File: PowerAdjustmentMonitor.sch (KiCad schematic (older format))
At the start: 37 parts, among them U6 LM317, U7 LM317, U8 LM337T, U9 LM337T

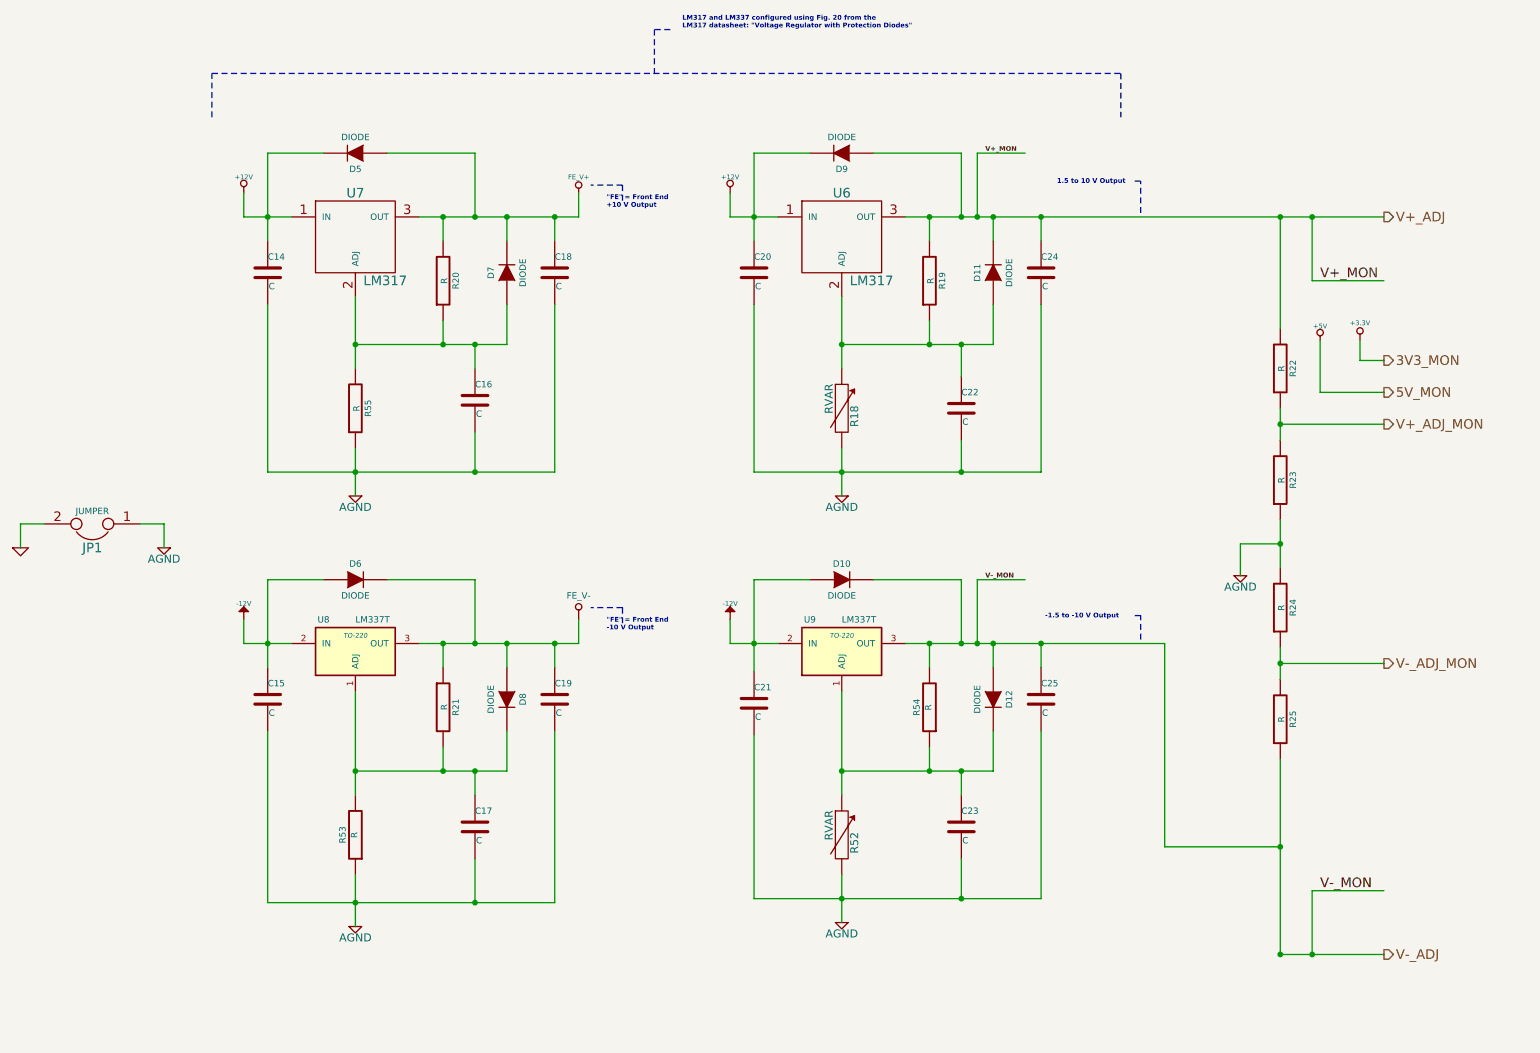
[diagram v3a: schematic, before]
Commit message: Association and layout of the power regulator mod
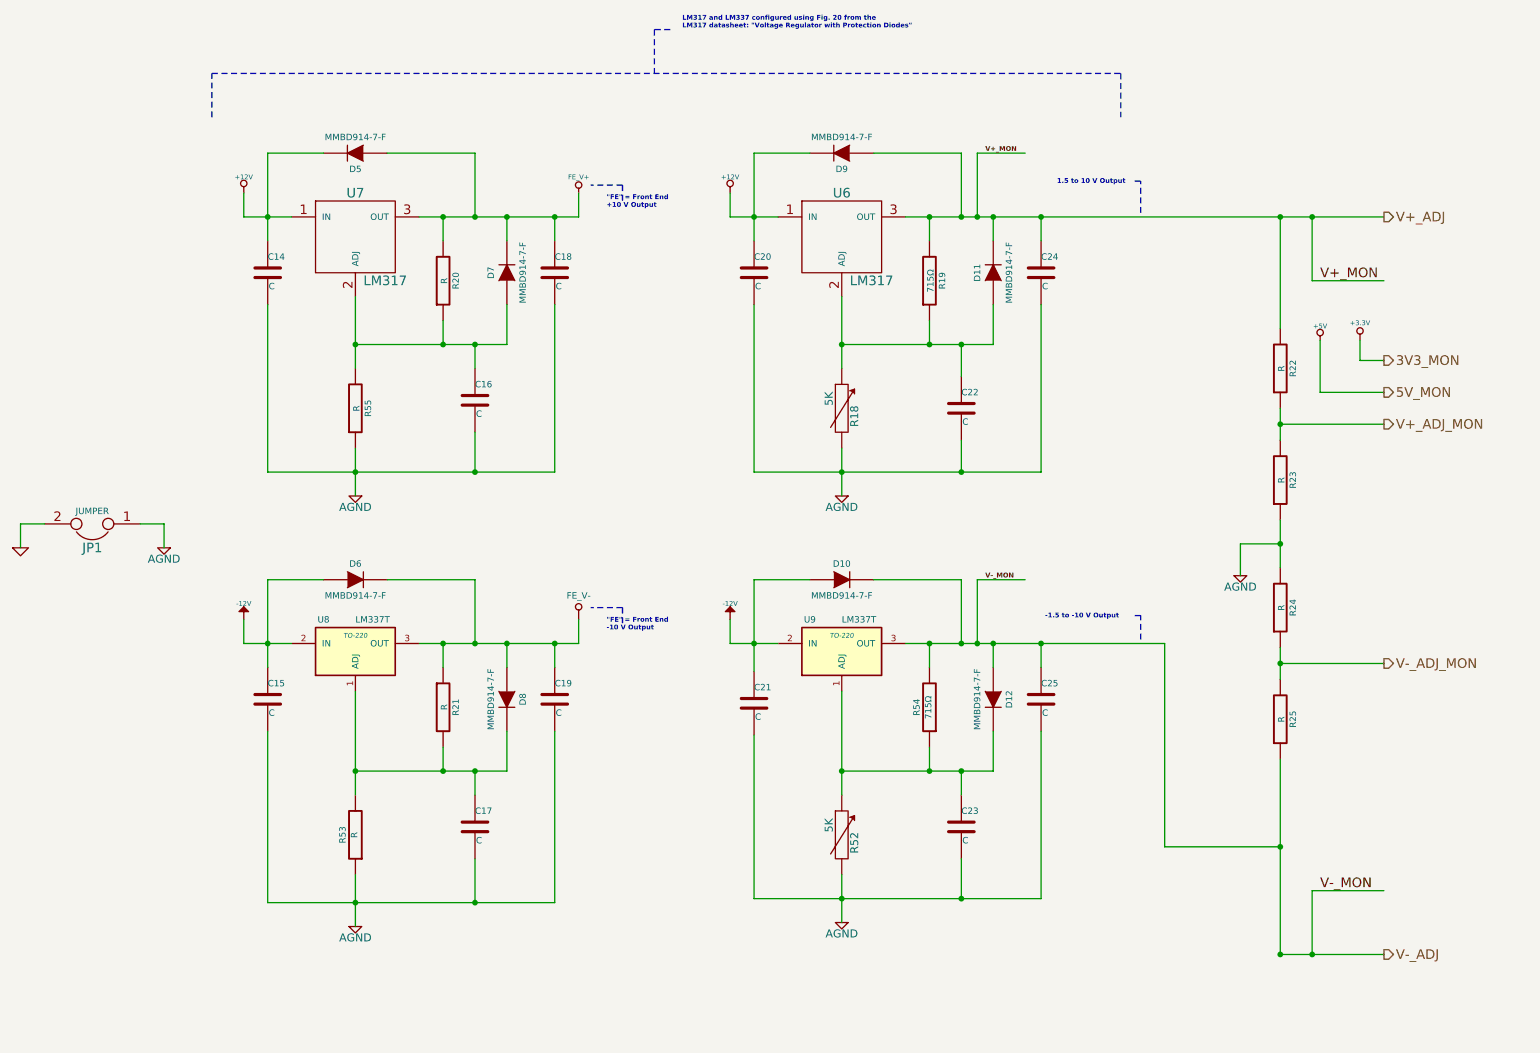
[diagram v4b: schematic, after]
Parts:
- D10, D11, D12, D5, D6, D7, D8, D9: value DIODE -> MMBD914-7-F
- R18, R52: value RVAR -> 5K; Distrib Part Num 1 (none) -> P3W1502; MFG Name (none) -> Panasonic Electronic Components; MFG Part Num (none) -> EVU-E3KFK4B53
- R19, R54: value R -> 715Ω
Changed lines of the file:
@@
 Sheet 6 9
 Title ""
-Date "22 feb 2014"
+Date "23 feb 2014"
 Rev ""
 Comp ""
@@
 P 6375 2350
 F 0 "R19" V 6455 2350 40  0000 C CNN
-F 1 "R" V 6382 2351 40  0000 C CNN
+F 1 "715Ω" V 6382 2351 40  0000 C CNN
 F 2 "~" V 6305 2350 30  0000 C CNN
 F 3 "~" H 6375 2350 30  0000 C CNN
@@
 P 5825 3150
 F 0 "R18" V 5905 3100 50  0000 C CNN
-F 1 "RVAR" V 5745 3210 50  0000 C CNN
+F 1 "5K" V 5745 3210 50  0000 C CNN
 F 2 "~" H 5825 3150 60  0000 C CNN
 F 3 "~" H 5825 3150 60  0000 C CNN
+F 4 "Panasonic Electronic Components" H 5825 3150 60  0001 C CNN "MFG Name"
+F 5 "EVU-E3KFK4B53" H 5825 3150 60  0001 C CNN "MFG Part Num"
+F 6 "P3W1502" H 5825 3150 60  0001 C CNN "Distrib Part Num 1"
 	1    5825 3150
 	1    0    0    -1
@@
 P 6375 5025
 F 0 "R54" V 6455 5025 40  0000 C CNN
-F 1 "R" V 6382 5026 40  0000 C CNN
+F 1 "715Ω" V 6382 5026 40  0000 C CNN
 F 2 "~" V 6305 5025 30  0000 C CNN
 F 3 "~" H 6375 5025 30  0000 C CNN
@@
 P 5825 5825
 F 0 "R52" V 5905 5775 50  0000 C CNN
-F 1 "RVAR" V 5745 5885 50  0000 C CNN
+F 1 "5K" V 5745 5885 50  0000 C CNN
 F 2 "~" H 5825 5825 60  0000 C CNN
 F 3 "~" H 5825 5825 60  0000 C CNN
+F 4 "Panasonic Electronic Components" H 5825 5825 60  0001 C CNN "MFG Name"
+F 5 "EVU-E3KFK4B53" H 5825 5825 60  0001 C CNN "MFG Part Num"
+F 6 "P3W1502" H 5825 5825 60  0001 C CNN "Distrib Part Num 1"
 	1    5825 5825
 	1    0    0    -1
@@
 P 2775 1550
 F 0 "D5" H 2775 1650 40  0000 C CNN
-F 1 "DIODE" H 2775 1450 40  0000 C CNN
+F 1 "MMBD914-7-F" H 2775 1450 40  0000 C CNN
 F 2 "~" H 2775 1550 60  0000 C CNN
 F 3 "~" H 2775 1550 60  0000 C CNN
@@
 P 3725 2300
 F 0 "D7" H 3725 2400 40  0000 C CNN
-F 1 "DIODE" H 3725 2200 40  0000 C CNN
+F 1 "MMBD914-7-F" H 3725 2200 40  0000 C CNN
 F 2 "~" H 3725 2300 60  0000 C CNN
 F 3 "~" H 3725 2300 60  0000 C CNN
@@
 P 2775 4225
 F 0 "D6" H 2775 4325 40  0000 C CNN
-F 1 "DIODE" H 2775 4125 40  0000 C CNN
+F 1 "MMBD914-7-F" H 2775 4125 40  0000 C CNN
 F 2 "~" H 2775 4225 60  0000 C CNN
 F 3 "~" H 2775 4225 60  0000 C CNN
@@
 P 3725 4975
 F 0 "D8" H 3725 5075 40  0000 C CNN
-F 1 "DIODE" H 3725 4875 40  0000 C CNN
+F 1 "MMBD914-7-F" H 3725 4875 40  0000 C CNN
 F 2 "~" H 3725 4975 60  0000 C CNN
 F 3 "~" H 3725 4975 60  0000 C CNN
@@
 P 5825 4225
 F 0 "D10" H 5825 4325 40  0000 C CNN
-F 1 "DIODE" H 5825 4125 40  0000 C CNN
+F 1 "MMBD914-7-F" H 5825 4125 40  0000 C CNN
 F 2 "~" H 5825 4225 60  0000 C CNN
 F 3 "~" H 5825 4225 60  0000 C CNN
@@
 P 5825 1550
 F 0 "D9" H 5825 1650 40  0000 C CNN
-F 1 "DIODE" H 5825 1450 40  0000 C CNN
+F 1 "MMBD914-7-F" H 5825 1450 40  0000 C CNN
 F 2 "~" H 5825 1550 60  0000 C CNN
 F 3 "~" H 5825 1550 60  0000 C CNN
@@
 P 6775 2300
 F 0 "D11" H 6775 2400 40  0000 C CNN
-F 1 "DIODE" H 6775 2200 40  0000 C CNN
+F 1 "MMBD914-7-F" H 6775 2200 40  0000 C CNN
 F 2 "~" H 6775 2300 60  0000 C CNN
 F 3 "~" H 6775 2300 60  0000 C CNN
@@
 P 6775 4975
 F 0 "D12" H 6775 5075 40  0000 C CNN
-F 1 "DIODE" H 6775 4875 40  0000 C CNN
+F 1 "MMBD914-7-F" H 6775 4875 40  0000 C CNN
 F 2 "~" H 6775 4975 60  0000 C CNN
 F 3 "~" H 6775 4975 60  0000 C CNN
